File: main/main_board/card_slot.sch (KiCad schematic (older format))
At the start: 5 parts, among them P1 my_pcie_8x

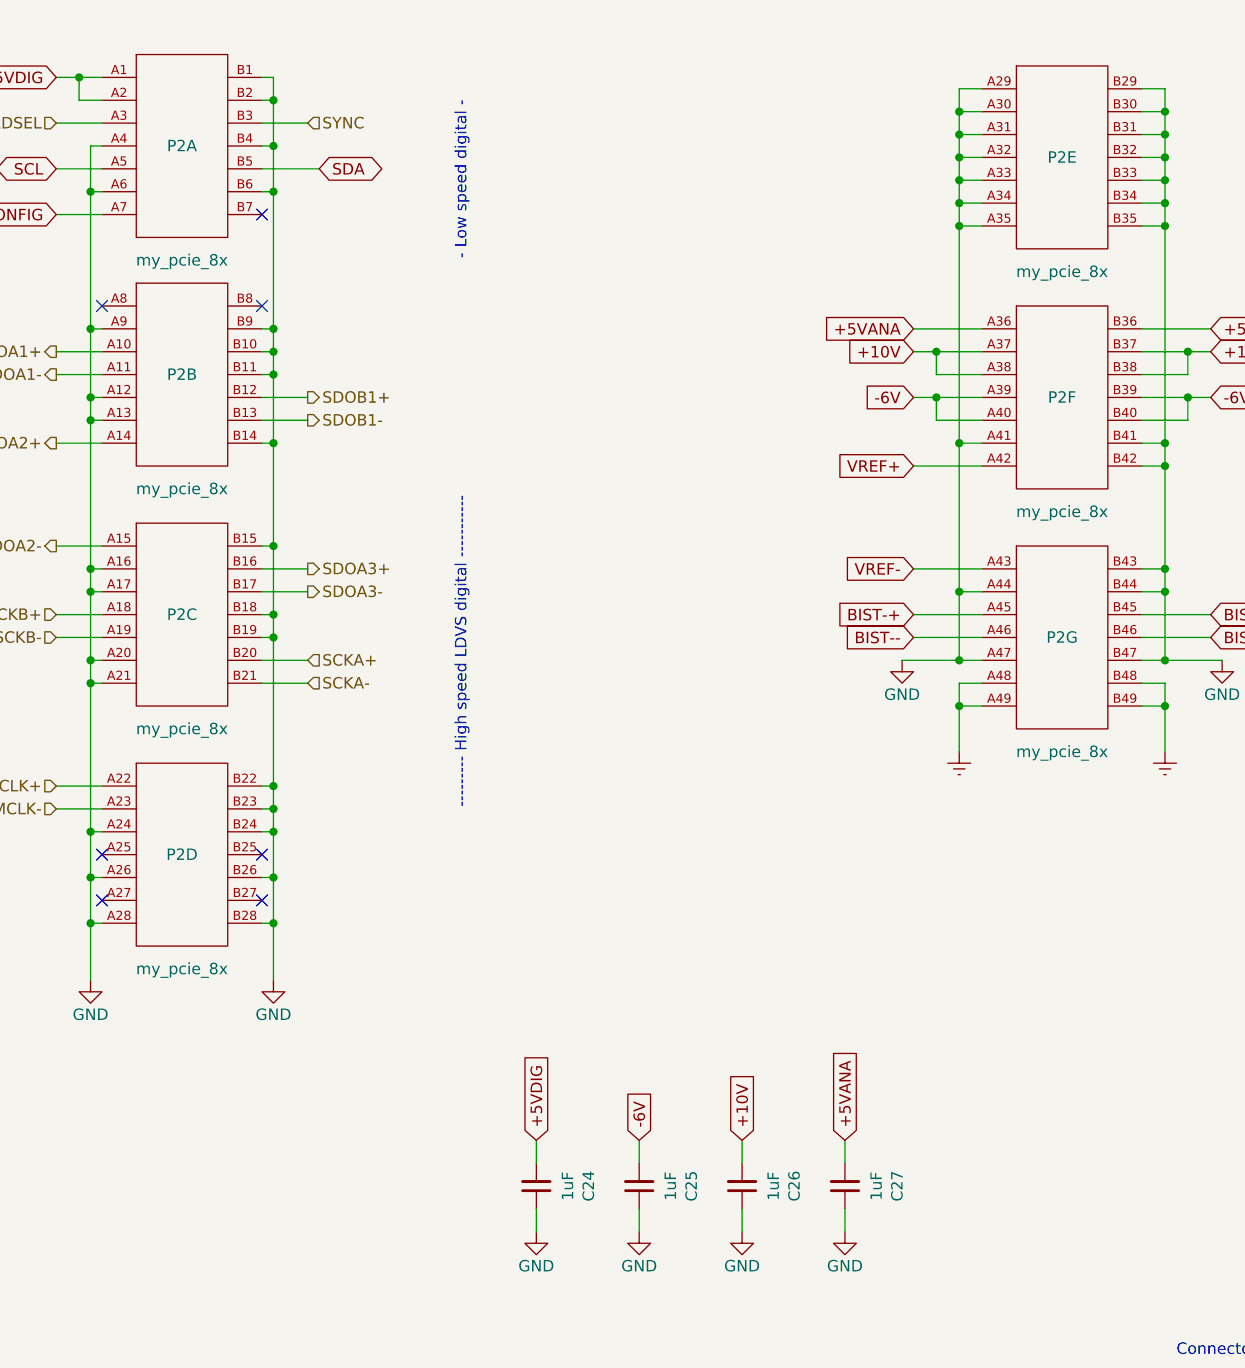
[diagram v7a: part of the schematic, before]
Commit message: Mostly work on main board layout. Aligned things on mm grid for easier routing, moved things around to create routing area. Neatened up component groups onto the grid. Parts of the routing plan are now drawn on the PCB.  See also notebook.txt. Reduced pad size of the PCIE connector, tweaked design rule clearances. Minor schematic tweaks.
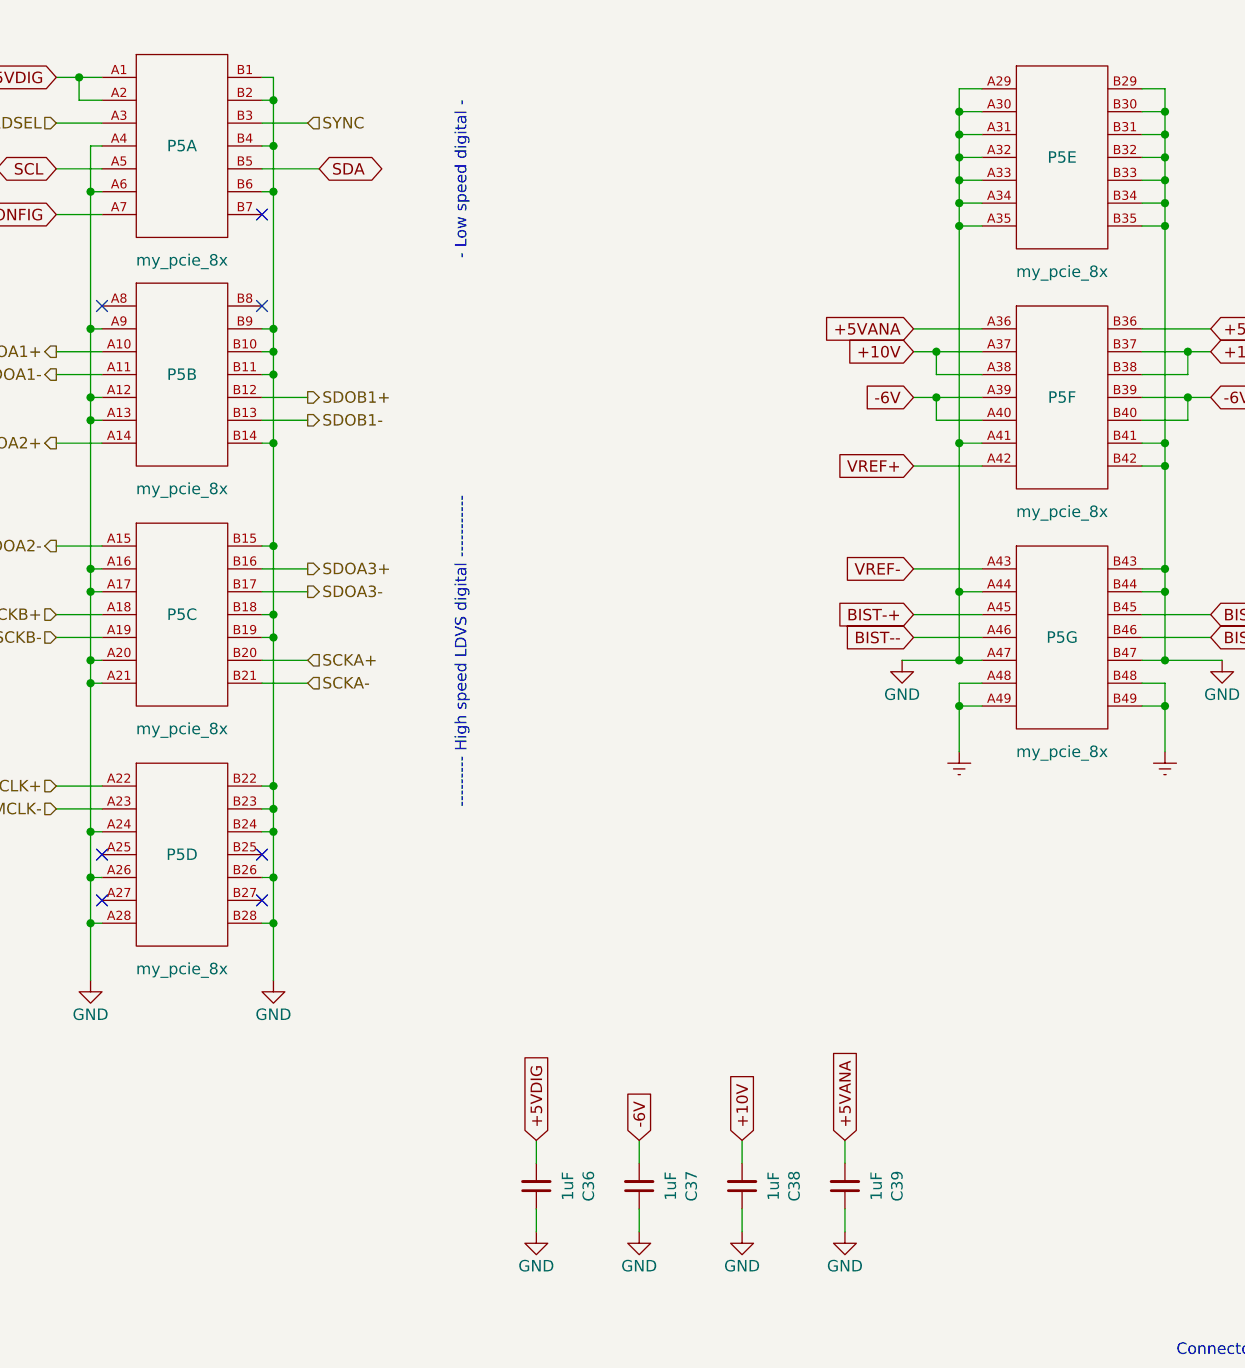
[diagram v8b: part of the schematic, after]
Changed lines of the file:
@@
 $Descr A4 11693 8268
 encoding utf-8
-Sheet 7 12
+Sheet 10 12
 Title ""
 Date ""
@@
 AR Path="/5E525FFE/5EBAAF8F/5E67C68B" Ref="P4"  Part="3"
 AR Path="/5E525FFE/5EBAAFA1/5E67C68B" Ref="P5"  Part="3"
-F 0 "P2" H 2900 3550 50  0000 C CNN
+F 0 "P5" H 2900 3550 50  0000 C CNN
 F 1 "my_pcie_8x" H 2900 3050 50  0000 C CNN
 F 2 "input:PCIE_8x_female" H 2900 4050 50  0001 C CNN
@@
 AR Path="/5E525FFE/5EBAAF8F/5E682A6A" Ref="P4"  Part="5"
 AR Path="/5E525FFE/5EBAAFA1/5E682A6A" Ref="P5"  Part="5"
-F 0 "P2" H 6750 1550 50  0000 C CNN
+F 0 "P5" H 6750 1550 50  0000 C CNN
 F 1 "my_pcie_8x" H 6750 1050 50  0000 C CNN
 F 2 "input:PCIE_8x_female" H 6750 2050 50  0001 C CNN
@@
 AR Path="/5E525FFE/5EBAAF8F/5E625DE8" Ref="P4"  Part="6"
 AR Path="/5E525FFE/5EBAAFA1/5E625DE8" Ref="P5"  Part="6"
-F 0 "P2" H 6750 2600 50  0000 C CNN
+F 0 "P5" H 6750 2600 50  0000 C CNN
 F 1 "my_pcie_8x" H 6750 2100 50  0000 C CNN
 F 2 "input:PCIE_8x_female" H 6750 3100 50  0001 C CNN
@@
 AR Path="/5E525FFE/5EBAAF8F/5E625DE9" Ref="P4"  Part="7"
 AR Path="/5E525FFE/5EBAAFA1/5E625DE9" Ref="P5"  Part="7"
-F 0 "P2" H 6750 3650 50  0000 C CNN
+F 0 "P5" H 6750 3650 50  0000 C CNN
 F 1 "my_pcie_8x" H 6750 3150 50  0000 C CNN
 F 2 "input:PCIE_8x_female" H 6750 4150 50  0001 C CNN
@@
 AR Path="/5E525FFE/5EBAAF8F/5EC152A6" Ref="P4"  Part="2"
 AR Path="/5E525FFE/5EBAAFA1/5EC152A6" Ref="P5"  Part="2"
-F 0 "P2" H 2900 2500 50  0000 C CNN
+F 0 "P5" H 2900 2500 50  0000 C CNN
 F 1 "my_pcie_8x" H 2900 2000 50  0000 C CNN
 F 2 "input:PCIE_8x_female" H 2900 3000 50  0001 C CNN
@@
 AR Path="/5E525FFE/5EBAAF8F/5E681104" Ref="P4"  Part="1"
 AR Path="/5E525FFE/5EBAAFA1/5E681104" Ref="P5"  Part="1"
-F 0 "P2" H 2900 1500 50  0000 C CNN
+F 0 "P5" H 2900 1500 50  0000 C CNN
 F 1 "my_pcie_8x" H 2900 1000 50  0000 C CNN
 F 2 "input:PCIE_8x_female" H 2900 2000 50  0001 C CNN
@@
 AR Path="/5E525FFE/5EBAAF8F/5EC152A7" Ref="P4"  Part="4"
 AR Path="/5E525FFE/5EBAAFA1/5EC152A7" Ref="P5"  Part="4"
-F 0 "P2" H 2900 4600 50  0000 C CNN
+F 0 "P5" H 2900 4600 50  0000 C CNN
 F 1 "my_pcie_8x" H 2900 4100 50  0000 C CNN
 F 2 "input:PCIE_8x_female" H 2900 5100 50  0001 C CNN
@@
 AR Path="/5E525FFE/5EBAAF8F/5ED81315" Ref="C32"  Part="1"
 AR Path="/5E525FFE/5EBAAFA1/5ED81315" Ref="C36"  Part="1"
-F 0 "C24" V 4221 6050 50  0000 C CNN
+F 0 "C36" V 4221 6050 50  0000 C CNN
 F 1 "1uF" V 4312 6050 50  0000 C CNN
 F 2 "Capacitor_SMD:C_0805_2012Metric" H 4450 6050 50  0001 C CNN
@@
 AR Path="/5E525FFE/5EBAAF8F/5EDA5F14" Ref="C33"  Part="1"
 AR Path="/5E525FFE/5EBAAFA1/5EDA5F14" Ref="C37"  Part="1"
-F 0 "C25" V 4671 6050 50  0000 C CNN
+F 0 "C37" V 4671 6050 50  0000 C CNN
 F 1 "1uF" V 4762 6050 50  0000 C CNN
 F 2 "Capacitor_SMD:C_0805_2012Metric" H 4900 6050 50  0001 C CNN
@@
 AR Path="/5E525FFE/5EBAAF8F/5EDBD896" Ref="C34"  Part="1"
 AR Path="/5E525FFE/5EBAAFA1/5EDBD896" Ref="C38"  Part="1"
-F 0 "C26" V 5121 6050 50  0000 C CNN
+F 0 "C38" V 5121 6050 50  0000 C CNN
 F 1 "1uF" V 5212 6050 50  0000 C CNN
 F 2 "Capacitor_SMD:C_0805_2012Metric" H 5350 6050 50  0001 C CNN
@@
 AR Path="/5E525FFE/5EBAAF8F/5EDCC5E2" Ref="C35"  Part="1"
 AR Path="/5E525FFE/5EBAAFA1/5EDCC5E2" Ref="C39"  Part="1"
-F 0 "C27" V 5571 6050 50  0000 C CNN
+F 0 "C39" V 5571 6050 50  0000 C CNN
 F 1 "1uF" V 5662 6050 50  0000 C CNN
 F 2 "Capacitor_SMD:C_0805_2012Metric" H 5800 6050 50  0001 C CNN
